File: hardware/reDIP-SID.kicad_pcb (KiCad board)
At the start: 4 copper layers, 17.8 x 38.1 mm, 100 parts, among them J1 Conn_01x01, J2 Conn_01x05, J3 Conn_01x14, J4 Conn_01x10, J5 TYPE-C-31-M-12, J6 Conn_02x05_Odd_Even, SW1 KXT331LHS, U1 NCP115AMX120TCG, U10 ICE40UP5K-SG48I, U2 NCP167AMX330TBG, U3 NCP115AMX120TCG, U4 SN74CBTD16211DGVR, U5 SGTL5000XNLA3, U6 NUF2042XV6, U7 MCP6H01T-E/OT, U8 LY68L6400SLIT, U9 W25Q128JVPIM, X1 ASCO-24.000MHZ-EK-T3

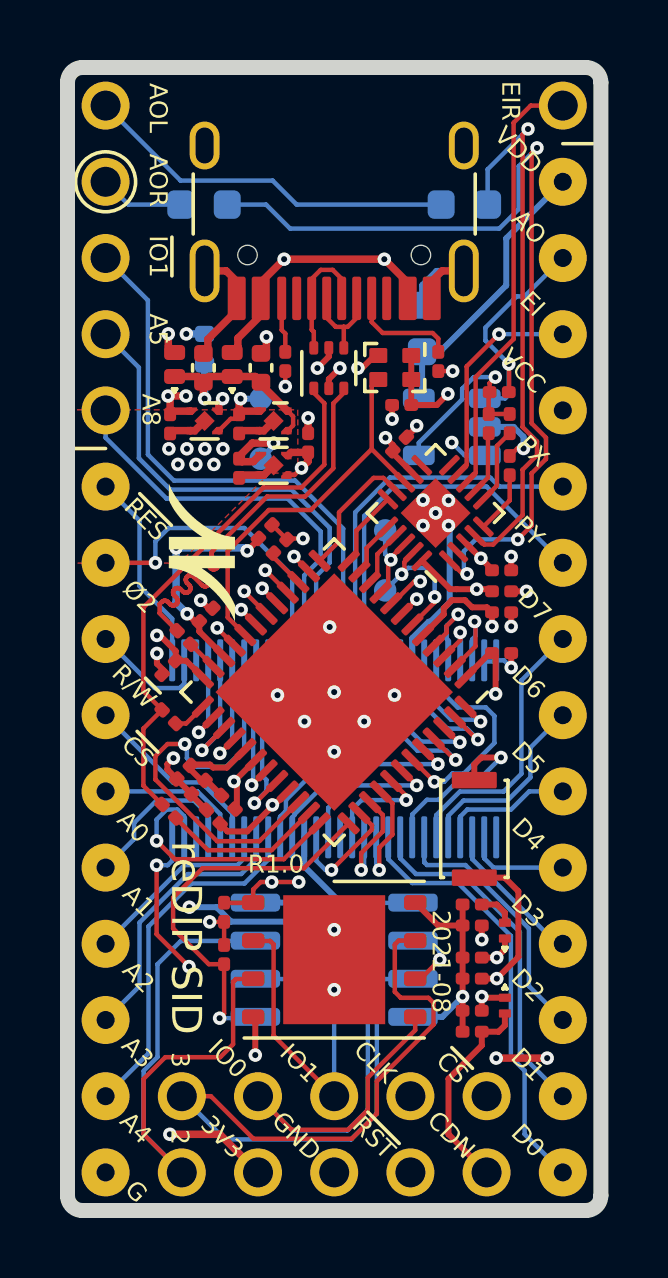
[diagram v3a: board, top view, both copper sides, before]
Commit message: Final major changes
* Replaced Schottky diodes with power switch, minimizing 5V rail voltage drop.
* Allow for measurement of VDD on SGTL5000 MIC input, as suggested by @smunaut.
* Adjustments to the USB-C receptacle footprint, based on 2015 and 2020
  HRO TYPE-C-31-M-12 drawings, and the 2019 GCT USB4105 drawing.
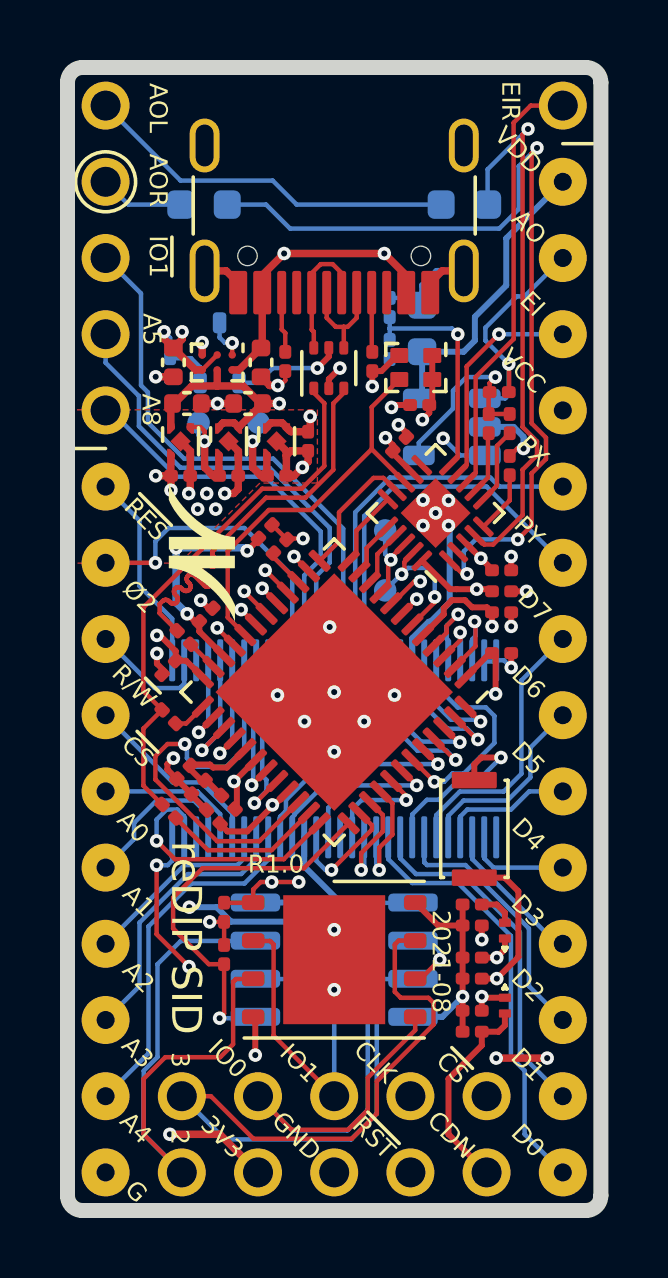
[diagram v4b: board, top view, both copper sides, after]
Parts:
- removed the D2 at (102.3, 106.1)
- removed JP1: SolderJumper_2_Open, reDIP:DNP_0402_1005Metric
- removed the R10 at (105.3, 111.7)
- removed the R4 at (112.8, 108.1)
- removed the SolderMask_D0.3mm at (102.4, 109.4)
- removed the SolderMask_D0.3mm at (103.9, 108.9)
- removed the SolderMask_D0.3mm at (103.3, 108.9)
- removed the SolderMask_D0.3mm at (102.7, 108.9)
- removed the SolderMask_D0.3mm at (102.1, 108.9)
- removed the SolderMask_D0.3mm at (103.6, 109.4)
- removed the SolderMask_D0.3mm at (103.0, 109.4)
- removed the SolderMask_D0.5mm at (103.0, 109.4)
- removed the SolderMask_D0.5mm at (102.4, 109.4)
- removed the SolderMask_D0.5mm at (102.1, 108.9)
- removed the SolderMask_D0.5mm at (102.7, 108.9)
- removed the SolderMask_D0.5mm at (103.3, 108.9)
- removed the SolderMask_D0.5mm at (103.6, 109.4)
- removed the SolderMask_D0.5mm at (103.9, 108.9)
- added C7: 1uF, Capacitor_SMD:C_0201_0603Metric, F.Cu at (106.8, 108.7)
- added C8: 1uF, Capacitor_SMD:C_0201_0603Metric, F.Cu at (105.7, 109.8)
- added R1: 20k, Resistor_SMD:R_0201_0603Metric, B.Cu at (102.2, 106.2)
- added R13: 10k, Resistor_SMD:R_0201_0603Metric, F.Cu at (105.3, 111.7)
- added R5: 402k, Resistor_SMD:R_0201_0603Metric, B.Cu at (109.5, 105.6)
- added R6: 20k, Resistor_SMD:R_0201_0603Metric, F.Cu at (112.8, 108.1)
- added R8: 100k, Resistor_SMD:R_0201_0603Metric, B.Cu at (109.5, 104.2)
- added SolderMask_D0.3mm: SolderMask_D0.3mm, reDIP:SolderMask_D0.3mm, F.Cu at (104.0, 110.4)
- added SolderMask_D0.3mm: SolderMask_D0.3mm, reDIP:SolderMask_D0.3mm, F.Cu at (103.4, 110.4)
- added SolderMask_D0.3mm: SolderMask_D0.3mm, reDIP:SolderMask_D0.3mm, F.Cu at (102.8, 110.4)
- added SolderMask_D0.3mm: SolderMask_D0.3mm, reDIP:SolderMask_D0.3mm, F.Cu at (103.7, 110.9)
- added SolderMask_D0.3mm: SolderMask_D0.3mm, reDIP:SolderMask_D0.3mm, F.Cu at (103.1, 110.9)
- added SolderMask_D0.5mm: SolderMask_D0.5mm, reDIP:SolderMask_D0.5mm, B.Cu at (103.1, 110.9)
- added SolderMask_D0.5mm: SolderMask_D0.5mm, reDIP:SolderMask_D0.5mm, B.Cu at (102.8, 110.4)
- added SolderMask_D0.5mm: SolderMask_D0.5mm, reDIP:SolderMask_D0.5mm, B.Cu at (103.4, 110.4)
- added SolderMask_D0.5mm: SolderMask_D0.5mm, reDIP:SolderMask_D0.5mm, B.Cu at (103.7, 110.9)
- added SolderMask_D0.5mm: SolderMask_D0.5mm, reDIP:SolderMask_D0.5mm, B.Cu at (104.0, 110.4)
- added U4: FPF1321UCX, ONSemi:CASE567RM_1.46x0.96mm_P0.5mm, F.Cu at (103.7, 106.0)
- C2, C5: footprint Capacitor_SMD:C_0201_0603Metric -> Capacitor_SMD:C_0402_1005Metric
- D1: value PMEG2010BELD -> BAV70W; footprint Nexperia:D_SOD-882D -> reDIP:SOT-323_SC-70; moved to B.Cu
- SW1: value KXT331LHS -> KXT311LHS
- moved C5 4.25 mm to (102.7, 107.4), turned to 0 degrees
- moved C1 2.93 mm to (102.3, 106.0), turned to 270 degrees
- moved C4 2.61 mm to (104.1, 109.8), turned to 0 degrees
- moved TP1 2.23 mm to (103.1, 108.1)
- moved R11 2.20 mm to (108.9, 106.0)
- moved C2 2.18 mm to (105.2, 106.0)
- moved C6 1.97 mm to (102.5, 109.8), turned to 0 degrees
- moved C3 1.91 mm to (104.8, 107.4), turned to 180 degrees
- moved U1 1.65 mm to (104.1, 108.7), turned to 90 degrees
- moved TP2 1.18 mm to (105.1, 108.0)
- moved U2 1.05 mm to (102.5, 108.7), turned to 90 degrees
- moved U3 0.81 mm to (105.7, 108.7), turned to 90 degrees
- moved X1 0.70 mm to (110.3, 106.2)
- moved C25 0.60 mm to (110.5, 107.4)
- moved D1 0.57 mm to (103.8, 105.7)
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- renumbered C8 to C10, C9 to C11, C10 to C12, C11 to C13, C12 to C14, C13 to C15, C14 to C16, C15 to C17, C16 to C18, C17 to C19, C18 to C20, C19 to C21, C20 to C22, C21 to C23, C22 to C24, C23 to C25, C7 to C9, D3 to D2, D4 to D3, R7 to R10, R8 to R11, R9 to R12, R11 to R14, R12 to R15, R13 to R16, R14 to R17, R15 to R18, R16 to R19, R1 to R2, R17 to R20, R2 to R3, R3 to R4, R5 to R7, R6 to R9, U9 to U10, U10 to U11, U4 to U5, U5 to U6, U6 to U7, U7 to U8, U8 to U9
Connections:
- C1 pad 1: +5V -> VCC
- C2 pad 1: +1V2 -> VBUS
- C4 pad 1: +3V3 -> +1V2
- C5 pad 1: +3V3 -> +5V
- C6 pad 1: VDDD -> +3V3
- D1 pad 1: +5V -> VBUS
- D1 pad 2: VBUS -> VCC
- U6 pad 10: (no net) -> Net-(R5-Pad1)
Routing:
- net VBUS: track 9.63 -> 17.6 mm
- net Net-(R5-Pad1): track 0.00 -> 7.59 mm, vias 0 -> 1
- net GND: track 50.1 -> 55.1 mm, vias 41 -> 40
- net VCC: track 22.7 -> 27.3 mm
- net +5V: track 38.0 -> 40.2 mm, vias 3 -> 2
- net Net-(J5-PadA5): track 3.68 -> 1.98 mm
- net VDD: track 9.52 -> 11.2 mm
- net Net-(D1-Pad3): track 0.00 -> 1.38 mm, vias 0 -> 1
- net +3V3: track 41.2 -> 40.2 mm
- net /~IO1~: track 19.1 -> 18.5 mm
- net /A5: track 17.1 -> 16.4 mm
- net /A8: track 13.9 -> 13.4 mm
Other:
- board text added: "tnt"
- board text removed: "pinout"

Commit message: Added back JP1
Thanks to @smunaut for the suggestion of jumpering VBUS and VCC
instead of 5V and VCC, making JP1 compatible with the power switch.
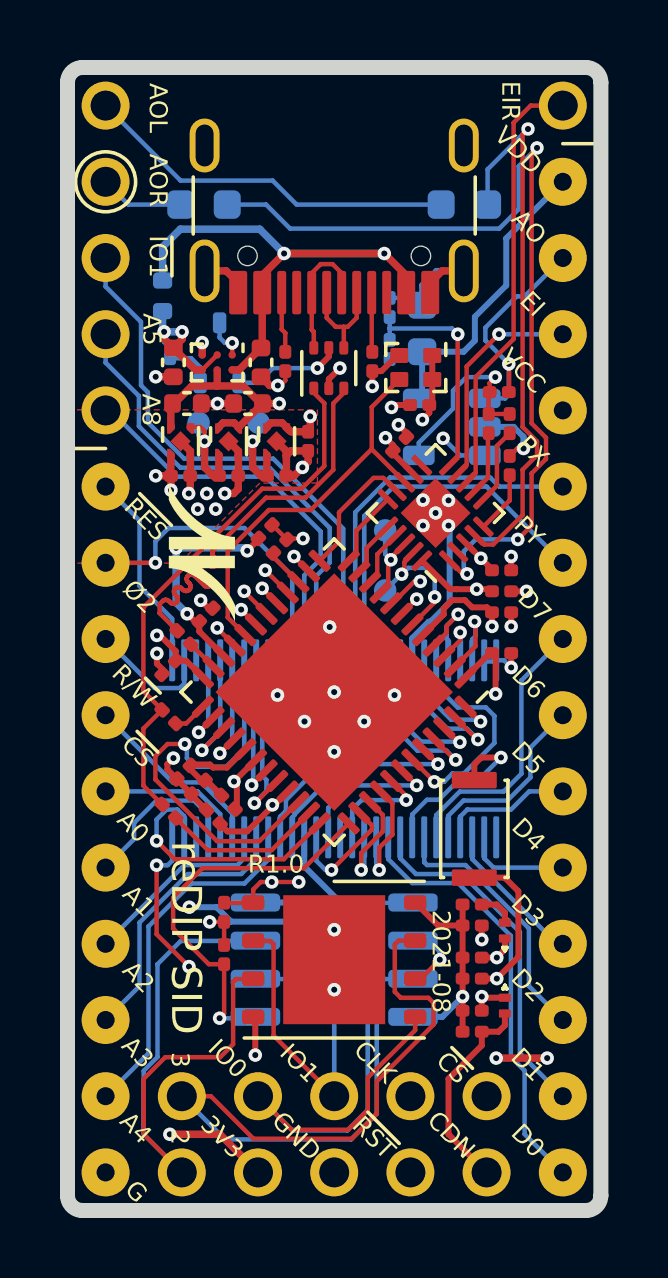
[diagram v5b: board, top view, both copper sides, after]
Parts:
- added JP1: SolderJumper_2_Open, reDIP:DNP_0402_1005Metric, B.Cu at (101.9, 103.8)
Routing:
- net VBUS: track 17.6 -> 26.7 mm
- net VCC: track 27.3 -> 28.6 mm

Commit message: Minor adjustments
* Increased hole diameter to 0.65mm for round pin headers
* Minor track and via cleanup
* Changed solder mask color to matte black
* README updates
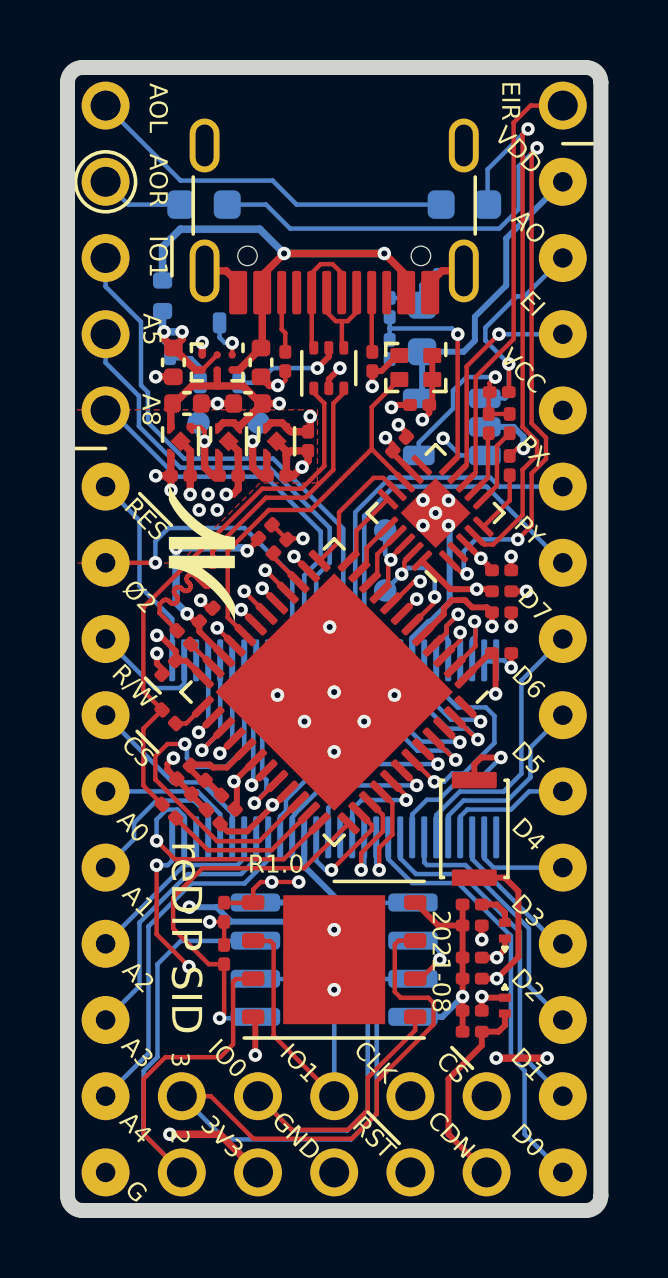
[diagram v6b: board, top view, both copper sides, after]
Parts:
- moved SolderMask_D0.3mm 0.06 mm to (103.1, 110.9)
- moved SolderMask_D0.5mm 0.06 mm to (103.1, 110.9)
- moved SolderMask_D0.3mm 0.06 mm to (104.0, 110.4)
- moved SolderMask_D0.3mm 0.06 mm to (103.4, 110.4)
- moved SolderMask_D0.3mm 0.06 mm to (102.8, 110.4)
- moved SolderMask_D0.3mm 0.06 mm to (103.7, 110.9)
- moved SolderMask_D0.5mm 0.06 mm to (102.8, 110.4)
- moved SolderMask_D0.5mm 0.06 mm to (103.4, 110.4)
- moved SolderMask_D0.5mm 0.06 mm to (103.7, 110.9)
- moved SolderMask_D0.5mm 0.06 mm to (104.0, 110.4)

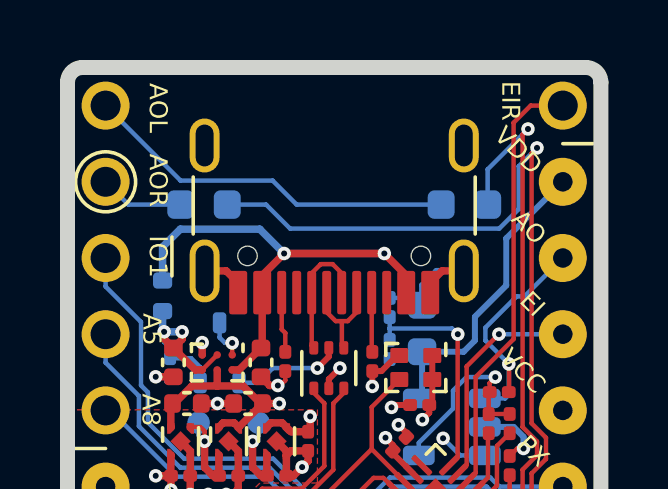
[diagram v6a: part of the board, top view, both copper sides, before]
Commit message: Added silkscreen polarity marking for tantalum capacitors
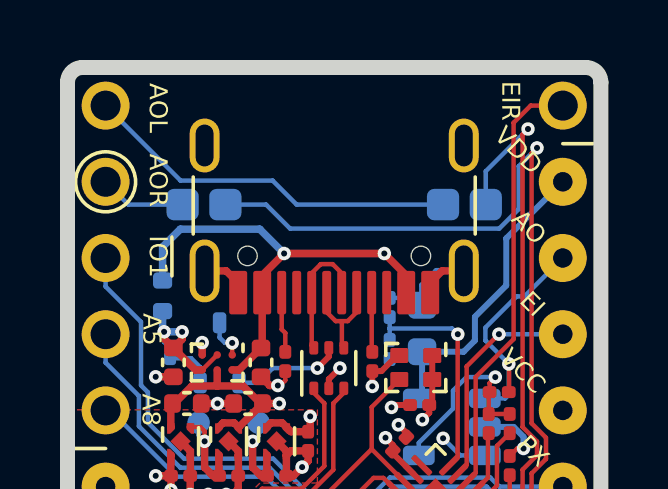
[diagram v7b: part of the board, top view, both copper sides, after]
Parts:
- C14, C15: footprint Capacitor_SMD:C_0603_1608Metric -> Capacitor_Tantalum_SMD:CP_EIA-1608-08_AVX-J

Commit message: Updated PCB from Schematic wrt. change of (invisible) resistor value
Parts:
- R14: value 1.5k -> 2.2k
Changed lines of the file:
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@@
       (effects (font (size 1 1) (thickness 0.15)) (justify mirror))
-    )
-    (fp_text user %R (at 0 0) (layer B.Fab)
-      (effects (font (size 0.4 0.4) (thickness 0.06)) (justify mirror))
     )
     (fp_line (start 0.8 0.425) (end -0.5 0.425) (layer B.Fab) (width 0.1))
@@
     (fp_line (start 1.5 0.78) (end 1.5 -0.78) (layer B.CrtYd) (width 0.05))
     (fp_line (start 1.5 -0.78) (end -1.5 -0.78) (layer B.CrtYd) (width 0.05))
+    (fp_text user %R (at 0 0) (layer B.Fab)
+      (effects (font (size 0.4 0.4) (thickness 0.06)) (justify mirror))
+    )
     (pad 2 smd roundrect (at 0.7125 0 180) (size 1.075 1.05) (layers B.Cu B.Paste B.Mask) (roundrect_rratio 0.238095)
       (net 80 /AOUT_L))
@@
     (fp_text value 10uF (at 0 -1.48) (layer B.Fab) hide
       (effects (font (size 1 1) (thickness 0.15)) (justify mirror))
-    )
-    (fp_text user %R (at 0 0) (layer B.Fab)
-      (effects (font (size 0.4 0.4) (thickness 0.06)) (justify mirror))
     )
     (fp_line (start 0.8 0.425) (end -0.5 0.425) (layer B.Fab) (width 0.1))
@@
     (fp_line (start 1.5 0.78) (end 1.5 -0.78) (layer B.CrtYd) (width 0.05))
     (fp_line (start 1.5 -0.78) (end -1.5 -0.78) (layer B.CrtYd) (width 0.05))
+    (fp_text user %R (at 0 0) (layer B.Fab)
+      (effects (font (size 0.4 0.4) (thickness 0.06)) (justify mirror))
+    )
     (pad 2 smd roundrect (at 0.7125 0 180) (size 1.075 1.05) (layers B.Cu B.Paste B.Mask) (roundrect_rratio 0.238095)
       (net 79 /AOUT_R))
@@
     )
     (fp_text value Conn_01x14 (at 0 -35.35) (layer B.Fab) hide
-      (effects (font (size 1 1) (thickness 0.15)) (justify mirror))
-    )
-    (fp_text user %R (at 0 -16.51 270) (layer B.Fab)
       (effects (font (size 1 1) (thickness 0.15)) (justify mirror))
     )
@@
     (fp_line (start 1.27 1.27) (end 1.27 -34.29) (layer B.Fab) (width 0.1))
     (fp_line (start -0.635 1.27) (end 1.27 1.27) (layer B.Fab) (width 0.1))
+    (fp_text user %R (at 0 -16.51 270) (layer B.Fab)
+      (effects (font (size 1 1) (thickness 0.15)) (justify mirror))
+    )
     (pad 14 thru_hole circle (at 0 -33.02 180) (size 1.6 1.6) (drill 0.65) (layers *.Cu *.Mask)
       (net 18 /D0))
@@
       (effects (font (size 1 1) (thickness 0.15)) (justify mirror))
     )
-    (fp_text user %R (at 0 -11.43 270) (layer B.Fab)
-      (effects (font (size 1 1) (thickness 0.15)) (justify mirror))
-    )
     (fp_line (start -0.635 1.27) (end 1.27 1.27) (layer B.Fab) (width 0.1))
     (fp_line (start 1.27 1.27) (end 1.27 -24.13) (layer B.Fab) (width 0.1))
@@
     (fp_line (start 1.8 -24.66) (end 1.8 1.8) (layer B.CrtYd) (width 0.05))
     (fp_line (start 1.8 1.8) (end -1.8 1.8) (layer B.CrtYd) (width 0.05))
+    (fp_text user %R (at 0 -11.43 270) (layer B.Fab)
+      (effects (font (size 1 1) (thickness 0.15)) (justify mirror))
+    )
     (pad 10 thru_hole circle (at 0 -22.86 180) (size 1.6 1.6) (drill 0.65) (layers *.Cu *.Mask)
       (net 1 GND))
@@
       (effects (font (size 1 1) (thickness 0.15)))
     )
-    (fp_text value 1.5k (at 0 1.05) (layer F.Fab) hide
-      (effects (font (size 1 1) (thickness 0.15)))
-    )
+    (fp_text value 2.2k (at 0 1.05) (layer F.Fab) hide
+      (effects (font (size 1 1) (thickness 0.15)))
+    )
